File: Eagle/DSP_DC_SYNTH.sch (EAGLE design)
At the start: 84 parts, among them J16 U.FL_CONN, J17 U.FL_CONN, J2 3.5HEADPHONEJACK, J5 U.FL_CONN, J6 U.FL_CONN, U1 5V_REG, U2 MIXER, U3 DUAL_OP_AMP_LMV822, U4 DIGITAL_POTDIGITAL_POT, U5 TC1185-3.3VCT713, U6 LMX2326, U7 MAX2752, U8 RMK-3-93+

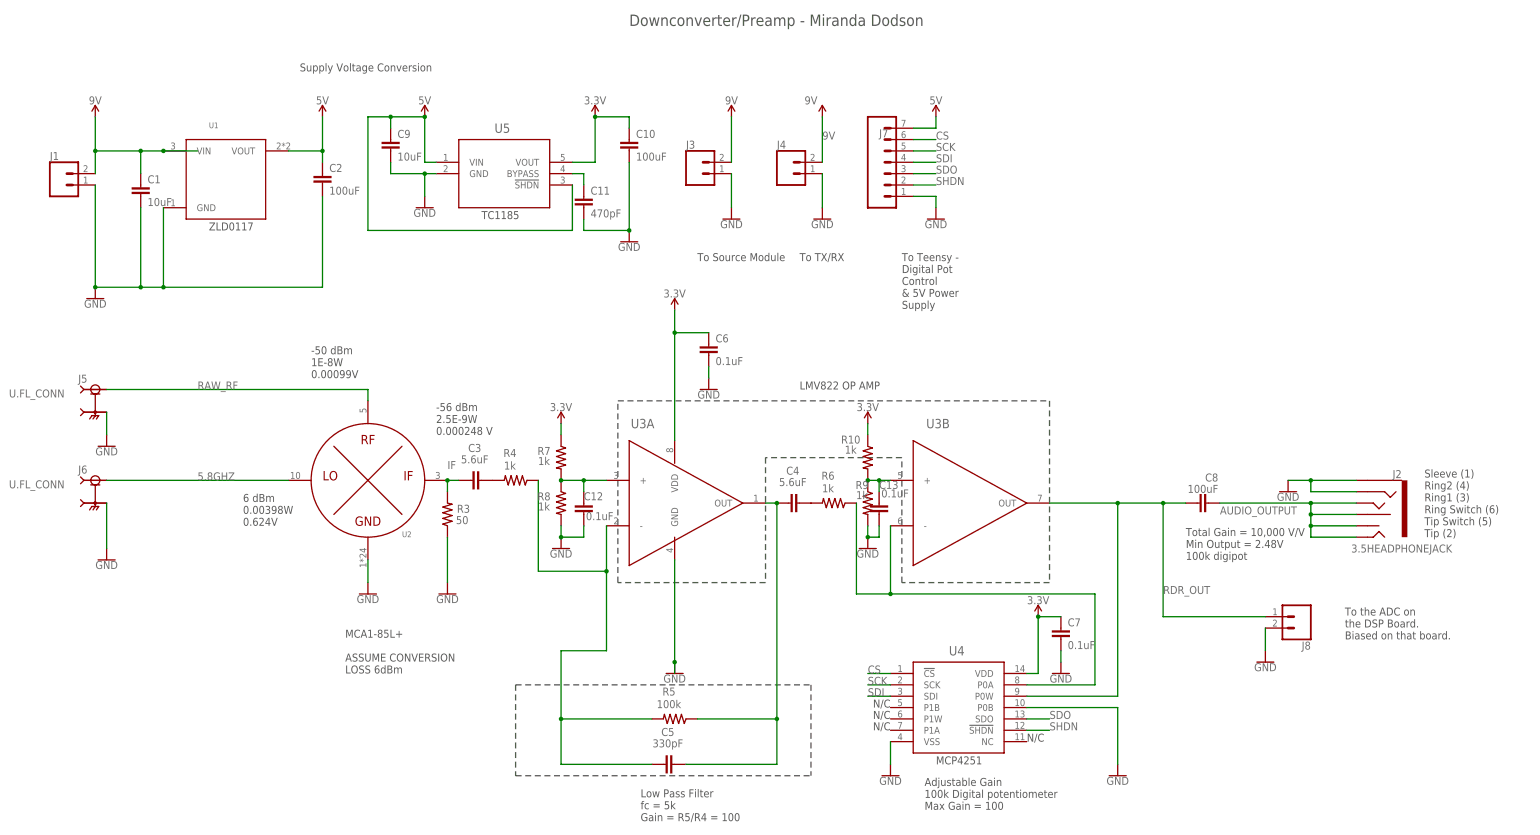
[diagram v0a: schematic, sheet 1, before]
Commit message: Updating Net Names to combine
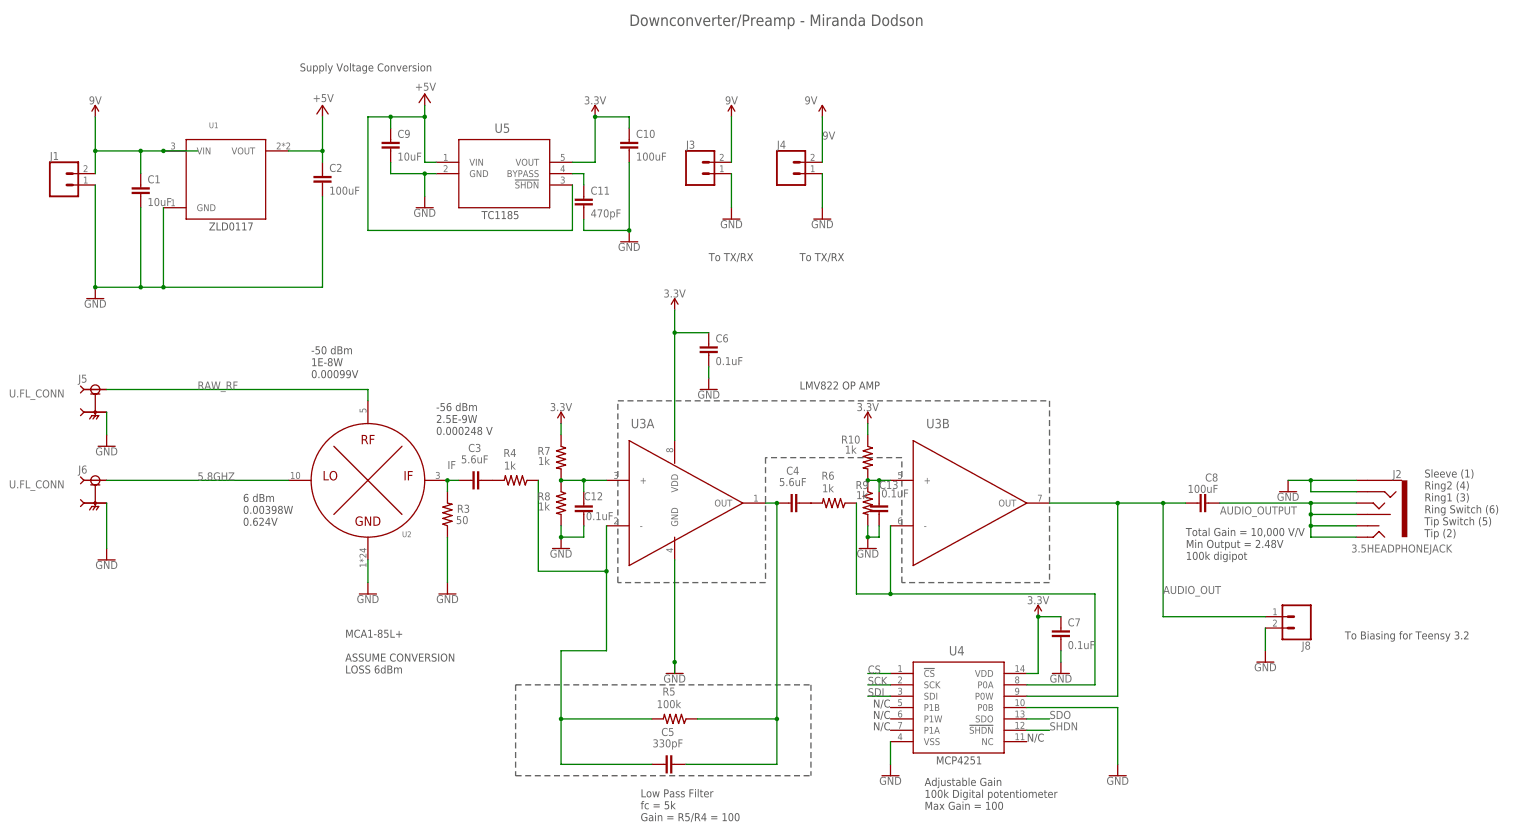
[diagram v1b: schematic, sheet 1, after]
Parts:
- removed J7: (no value), SparkFun-Connectors:CONN_07
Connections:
- net EXT_REF renamed N$39
- removed net 5V: C2.1, C9.1, J7.7, U1.VOUT, U5.!SHDN, U5.VIN
- removed net MULT_OUT: C22.2
- removed net RDR_IN: C18.1, J12.1
- removed net RDR_OUT: C8.1, J8.1, U3B.OUT, U4.P0W
- new net AUDIO_OUT: C18.1, C8.1, J12.1, J8.1, U3B.OUT, U4.P0W
- new net N$40: C22.2, J17.SIG
- net +5V: now also C2.1, C9.1, U1.VOUT, U5.!SHDN, U5.VIN
- net CS: no longer J7.6
- net GND: no longer J7.1
- net SCK: no longer J7.5
- net SDI: no longer J7.4
- net SDO: no longer J7.3
- net SHDN: no longer J7.2
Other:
- note added: "To Biasing for Teensy 3.2"
- note removed: "To Source Module"
- note removed: "To Teensy - Digital Pot Control & 5V Power Supply"
- note removed: "To the ADC on the DSP Board. Biased on that board."

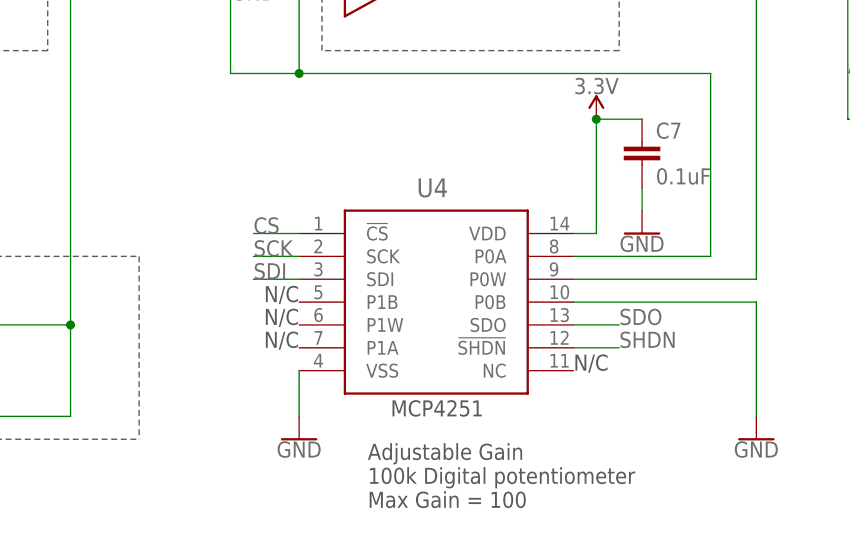
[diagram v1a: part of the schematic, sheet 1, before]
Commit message: Updated net names to match for zack's convention
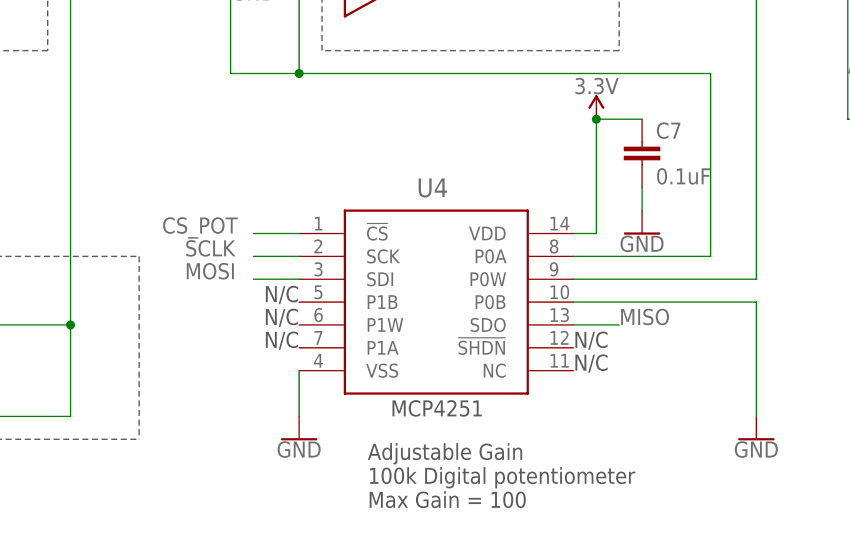
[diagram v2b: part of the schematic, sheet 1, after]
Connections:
- removed net CPOUT: U6.CPO
- removed net CS: U4.!CS
- removed net SCK: U4.SCK
- removed net SDI: U4.SDI
- removed net SDO: U4.SDO
- removed net SHDN: U4.!SHDN
- new net PLL_CLK: J14.4
- new net PLL_MOSI: J14.5
- net CP_OUT: now also U6.CPO
- net CS_POT: now also U4.!CS
- net MISO: now also U4.SDO
- net MOSI: now also U4.SDI
- net OSC_PLL_BU_EN: now also J14.3
- net PLL_LE: now also J14.6
- net SCLK: now also U4.SCK
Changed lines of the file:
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@@
 <text x="279.4" y="48.26" size="1.778" layer="97">To Biasing for Teensy 3.2</text>
 <text x="137.16" y="134.62" size="1.778" layer="97" align="top-left">To TX/RX</text>
+<text x="208.28" y="27.94" size="1.778" layer="97">N/C</text>
 </plain>
 <instances>
@@
 </segment>
 </net>
-<net name="CS" class="0">
+<net name="CS_POT" class="0">
 <segment>
 <pinref part="U4" gate="A" pin="!CS"/>
 <wire x1="177.8" y1="40.64" x2="172.72" y2="40.64" width="0.1524" layer="91"/>
-<label x="172.72" y="40.64" size="1.778" layer="95"/>
-</segment>
-</net>
-<net name="SCK" class="0">
+<label x="162.56" y="40.64" size="1.778" layer="95"/>
+</segment>
+</net>
+<net name="SCLK" class="0">
 <segment>
 <pinref part="U4" gate="A" pin="SCK"/>
 <wire x1="177.8" y1="38.1" x2="172.72" y2="38.1" width="0.1524" layer="91"/>
-<label x="172.72" y="38.1" size="1.778" layer="95"/>
-</segment>
-</net>
-<net name="SDI" class="0">
+<label x="165.1" y="38.1" size="1.778" layer="95"/>
+</segment>
+</net>
+<net name="MOSI" class="0">
 <segment>
 <pinref part="U4" gate="A" pin="SDI"/>
 <wire x1="177.8" y1="35.56" x2="172.72" y2="35.56" width="0.1524" layer="91"/>
-<label x="172.72" y="35.56" size="1.778" layer="95"/>
+<label x="165.1" y="35.56" size="1.778" layer="95"/>
 </segment>
 </net>
@@
 <wire x1="177.8" y1="73.66" x2="177.8" y2="58.42" width="0.1524" layer="91"/>
 <junction x="177.8" y="58.42"/>
-</segment>
-</net>
-<net name="SDO" class="0">
-<segment>
-<pinref part="U4" gate="A" pin="SDO"/>
-<wire x1="208.28" y1="30.48" x2="213.36" y2="30.48" width="0.1524" layer="91"/>
-<label x="213.36" y="30.48" size="1.778" layer="95"/>
-</segment>
-</net>
-<net name="SHDN" class="0">
-<segment>
-<pinref part="U4" gate="A" pin="!SHDN"/>
-<wire x1="208.28" y1="27.94" x2="213.36" y2="27.94" width="0.1524" layer="91"/>
-<label x="213.36" y="27.94" size="1.778" layer="95"/>
 </segment>
 </net>
@@
 <wire x1="73.66" y1="167.64" x2="73.66" y2="165.1" width="0.1524" layer="91"/>
 <junction x="73.66" y="165.1"/>
+</segment>
+</net>
+<net name="MISO" class="0">
+<segment>
+<pinref part="U4" gate="A" pin="SDO"/>
+<wire x1="208.28" y1="30.48" x2="213.36" y2="30.48" width="0.1524" layer="91"/>
+<label x="213.36" y="30.48" size="1.778" layer="95"/>
 </segment>
 </net>
@@
 </segment>
 </net>
-<net name="CPOUT" class="0">
-<segment>
-<pinref part="U6" gate="A" pin="CPO"/>
-<wire x1="220.98" y1="109.22" x2="223.52" y2="109.22" width="0.1524" layer="91"/>
-<label x="223.52" y="109.22" size="1.778" layer="95"/>
-</segment>
-</net>
 <net name="VCO_OUT" class="0">
 <segment>
@@
 <wire x1="25.4" y1="165.1" x2="30.48" y2="165.1" width="0.1524" layer="91"/>
 <label x="30.48" y="165.1" size="1.778" layer="95"/>
+<pinref part="J14" gate="G$1" pin="3"/>
 </segment>
 <segment>
@@
 <wire x1="30.48" y1="162.56" x2="25.4" y2="162.56" width="0.1524" layer="91"/>
 <label x="30.48" y="162.56" size="1.778" layer="95"/>
+<pinref part="J14" gate="G$1" pin="4"/>
 </segment>
 </net>
@@
 <wire x1="30.48" y1="160.02" x2="25.4" y2="160.02" width="0.1524" layer="91"/>
 <label x="30.48" y="160.02" size="1.778" layer="95"/>
+<pinref part="J14" gate="G$1" pin="5"/>
 </segment>
 </net>
@@
 <wire x1="30.48" y1="157.48" x2="25.4" y2="157.48" width="0.1524" layer="91"/>
 <label x="30.48" y="157.48" size="1.778" layer="95"/>
+<pinref part="J14" gate="G$1" pin="6"/>
 </segment>
 </net>
@@
 <label x="114.3" y="22.86" size="1.778" layer="95" rot="MR0"/>
 </segment>
+<segment>
+<pinref part="U6" gate="A" pin="CPO"/>
+<wire x1="220.98" y1="109.22" x2="223.52" y2="109.22" width="0.1524" layer="91"/>
+<label x="223.52" y="109.22" size="1.778" layer="95"/>
+</segment>
 </net>
 <net name="N$37" class="0">
@@
 </sheet>
 </sheets>
+<errors>
+</errors>
 </schematic>
 </drawing>

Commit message: started layout
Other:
- moved on the sheet: R10, R6, R9
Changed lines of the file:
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@@
 <attribute name="VALUE" x="128.27" y="33.782" size="1.778" layer="96" align="center"/>
 </instance>
-<instance part="R6" gate="G$1" x="165.1" y="78.74" smashed="yes" rot="R180">
-<attribute name="NAME" x="163.83" y="84.8614" size="1.778" layer="95" align="center"/>
-<attribute name="VALUE" x="163.83" y="82.042" size="1.778" layer="96" align="center"/>
+<instance part="R6" gate="G$1" x="162.56" y="78.74" smashed="yes" rot="R180">
+<attribute name="NAME" x="161.29" y="84.8614" size="1.778" layer="95" align="center"/>
+<attribute name="VALUE" x="161.29" y="82.042" size="1.778" layer="96" align="center"/>
 </instance>
 <instance part="C4" gate="G$1" x="154.94" y="78.74" smashed="yes" rot="R90">
@@
 <attribute name="VALUE" x="104.14" y="99.314" size="1.778" layer="96" align="bottom-center"/>
 </instance>
-<instance part="R9" gate="G$1" x="172.72" y="78.74" smashed="yes" rot="R270">
-<attribute name="NAME" x="171.45" y="82.7786" size="1.778" layer="95" rot="R180" align="center"/>
-<attribute name="VALUE" x="171.45" y="80.518" size="1.778" layer="96" rot="R180" align="center"/>
-</instance>
-<instance part="R10" gate="G$1" x="172.72" y="88.9" smashed="yes" rot="R270">
-<attribute name="NAME" x="168.91" y="92.9386" size="1.778" layer="95" rot="R180" align="center"/>
-<attribute name="VALUE" x="168.91" y="90.678" size="1.778" layer="96" rot="R180" align="center"/>
-</instance>
-<instance part="SUPPLY6" gate="G$1" x="172.72" y="96.52" smashed="yes">
-<attribute name="VALUE" x="172.72" y="99.314" size="1.778" layer="96" align="bottom-center"/>
+<instance part="R9" gate="G$1" x="170.18" y="78.74" smashed="yes" rot="R270">
+<attribute name="NAME" x="168.91" y="82.7786" size="1.778" layer="95" rot="R180" align="center"/>
+<attribute name="VALUE" x="168.91" y="80.518" size="1.778" layer="96" rot="R180" align="center"/>
+</instance>
+<instance part="R10" gate="G$1" x="170.18" y="88.9" smashed="yes" rot="R270">
+<attribute name="NAME" x="166.37" y="92.9386" size="1.778" layer="95" rot="R180" align="center"/>
+<attribute name="VALUE" x="166.37" y="90.678" size="1.778" layer="96" rot="R180" align="center"/>
+</instance>
+<instance part="SUPPLY6" gate="G$1" x="170.18" y="96.52" smashed="yes">
+<attribute name="VALUE" x="170.18" y="99.314" size="1.778" layer="96" align="bottom-center"/>
 </instance>
 <instance part="GND17" gate="1" x="172.72" y="68.58" smashed="yes">
@@
 <wire x1="129.54" y1="66.04" x2="129.54" y2="43.18" width="0.1524" layer="91"/>
 <pinref part="GND9" gate="1" pin="GND"/>
-<wire x1="129.54" y1="43.18" x2="129.54" y2="40.64" width="0.1524" layer="91"/>
-<junction x="129.54" y="43.18"/>
 </segment>
 <segment>
@@
 </segment>
 <segment>
-<pinref part="R9" gate="G$1" pin="2"/>
 <pinref part="GND17" gate="1" pin="GND"/>
-<wire x1="172.72" y1="73.66" x2="172.72" y2="71.12" width="0.1524" layer="91"/>
 <wire x1="172.72" y1="71.12" x2="175.26" y2="71.12" width="0.1524" layer="91"/>
-<junction x="172.72" y="71.12"/>
 <pinref part="C13" gate="G$1" pin="2"/>
 <wire x1="175.26" y1="71.12" x2="175.26" y2="73.66" width="0.1524" layer="91"/>
+<pinref part="R9" gate="G$1" pin="2"/>
+<wire x1="170.18" y1="73.66" x2="170.18" y2="71.12" width="0.1524" layer="91"/>
+<wire x1="170.18" y1="71.12" x2="172.72" y2="71.12" width="0.1524" layer="91"/>
+<junction x="172.72" y="71.12"/>
 </segment>
 </net>
@@
 <pinref part="C4" gate="G$1" pin="2"/>
 <pinref part="R6" gate="G$1" pin="2"/>
+<wire x1="157.48" y1="78.74" x2="160.02" y2="78.74" width="0.1524" layer="91"/>
 </segment>
 </net>
@@
 <segment>
 <pinref part="U3" gate="B" pin="+"/>
-<wire x1="172.72" y1="83.82" x2="175.26" y2="83.82" width="0.1524" layer="91"/>
+<wire x1="170.18" y1="83.82" x2="175.26" y2="83.82" width="0.1524" layer="91"/>
 <pinref part="R10" gate="G$1" pin="2"/>
 <pinref part="R9" gate="G$1" pin="1"/>
-<junction x="172.72" y="83.82"/>
+<junction x="170.18" y="83.82"/>
 <pinref part="C13" gate="G$1" pin="1"/>
 <wire x1="175.26" y1="83.82" x2="177.8" y2="83.82" width="0.1524" layer="91"/>
@@
 <wire x1="223.52" y1="58.42" x2="177.8" y2="58.42" width="0.1524" layer="91"/>
 <pinref part="R6" gate="G$1" pin="1"/>
-<wire x1="177.8" y1="58.42" x2="170.18" y2="58.42" width="0.1524" layer="91"/>
-<wire x1="170.18" y1="78.74" x2="170.18" y2="58.42" width="0.1524" layer="91"/>
+<wire x1="177.8" y1="58.42" x2="167.64" y2="58.42" width="0.1524" layer="91"/>
+<wire x1="167.64" y1="78.74" x2="167.64" y2="58.42" width="0.1524" layer="91"/>
 <pinref part="U3" gate="B" pin="-"/>
 <wire x1="177.8" y1="73.66" x2="177.8" y2="58.42" width="0.1524" layer="91"/>
@@
 <pinref part="R10" gate="G$1" pin="1"/>
 <pinref part="SUPPLY6" gate="G$1" pin="3.3V"/>
-<wire x1="172.72" y1="93.98" x2="172.72" y2="96.52" width="0.1524" layer="91"/>
-</segment>
-<segment>
+<wire x1="170.18" y1="93.98" x2="170.18" y2="96.52" width="0.1524" layer="91"/>
+</segment>
+<segment>
